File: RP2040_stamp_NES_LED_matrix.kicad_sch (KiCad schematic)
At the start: 11 parts

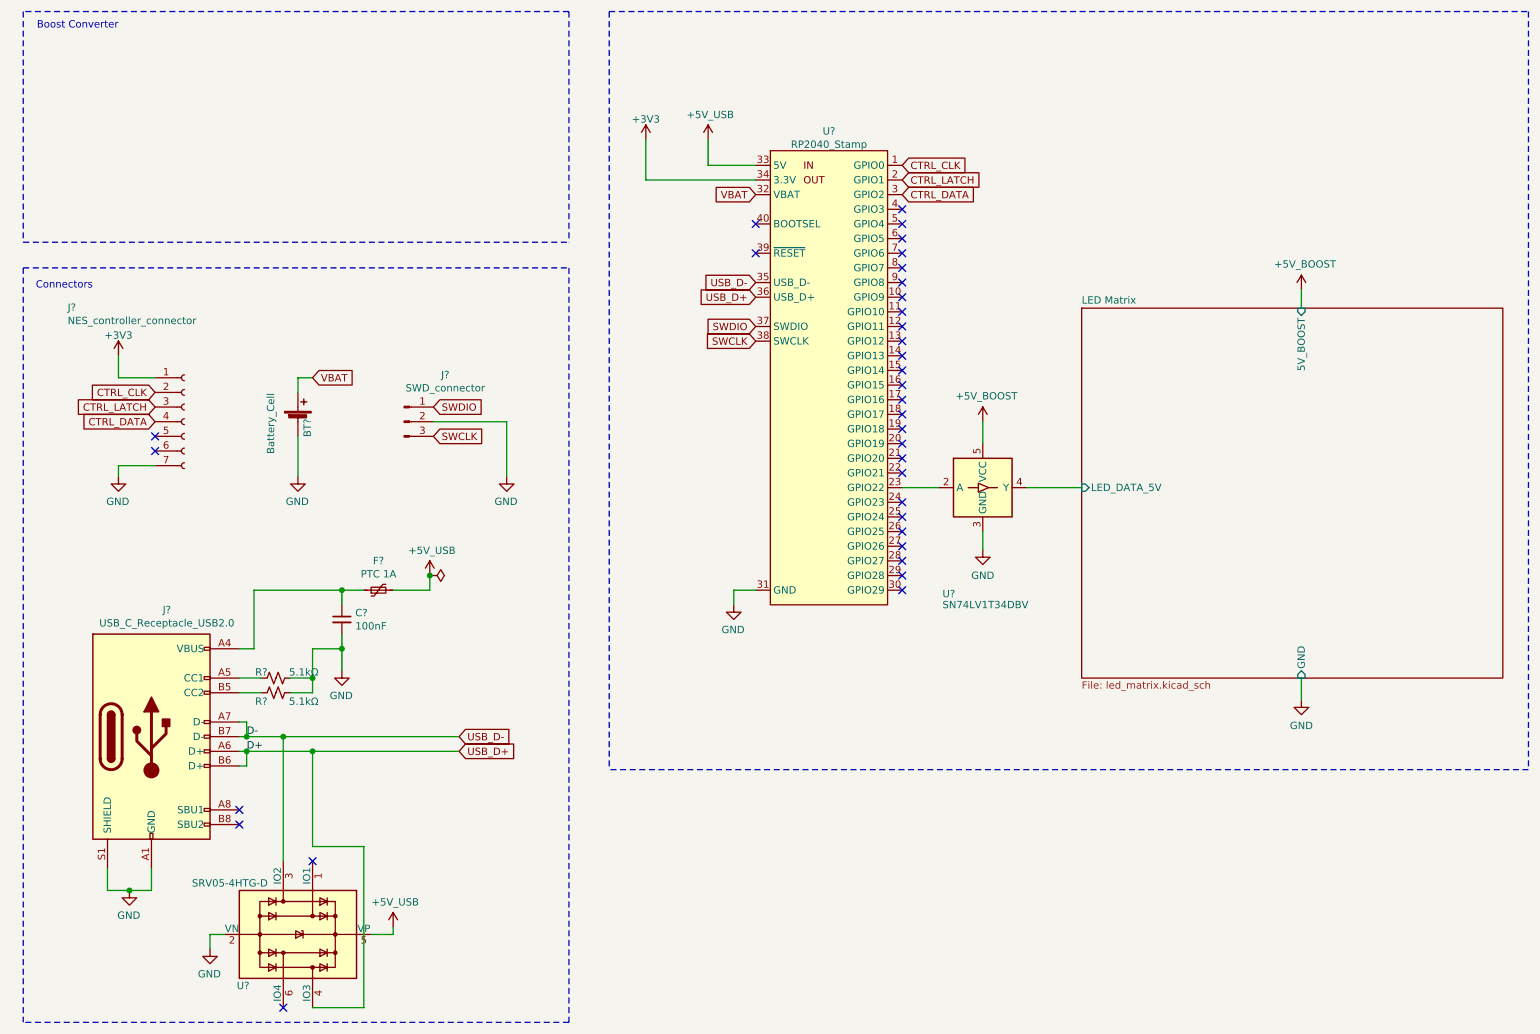
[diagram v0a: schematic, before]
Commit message: Removes boost converter placeholder since it won't be possible to use it
The stamp can only provide 500mA@3.3v, which gives us 1.65W. Assuming a
85% efficiency of the boost regulator, that would give us 1.4W on the
output, or 280mA@5V. We need 320mA to run the 64 WS2812C, so it doesn't
seem to be possible to run these from a LiPO battery unless we rely on
the software never running all the LEDs at full brightness, but that
doesn't seem like a reliable option.

We'll still use the WS2812C instead of the B for the lower power
consumption, though. Since we don't need a lot of brightness, running
the matrix with 320mA should make it possible for the whole thing to run
from a standard USB connection.
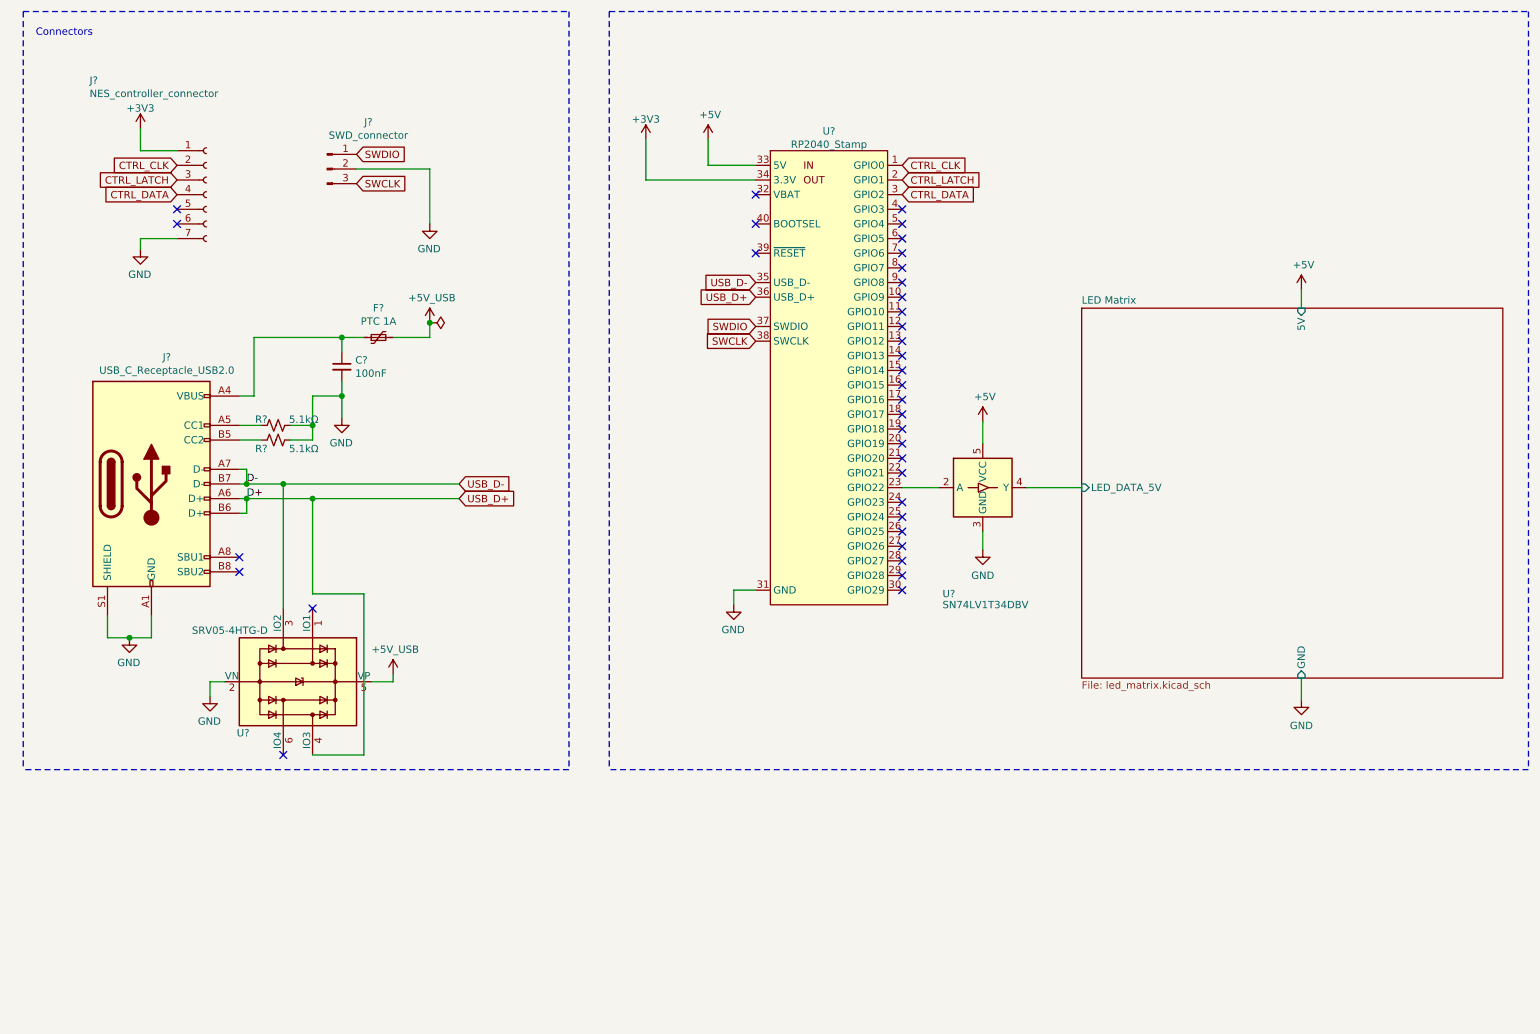
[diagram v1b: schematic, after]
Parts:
- removed BT?: Battery_Cell, Connector_JST:JST_PH_S2B-PH-SM4-TB_1x02-1MP_P2.00mm_Horizontal, symbol Device:Battery_Cell
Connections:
- net VBAT: no longer names the net of U?.32 (VBAT)
- no-connect marks 34 -> 35
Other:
- sheet LED Matrix ports: added 5V; removed 5V_BOOST
- note removed: "Boost Converter"
- moved on the sheet: C?, F?, J?, R?, U?
